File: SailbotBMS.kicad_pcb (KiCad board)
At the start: 2 copper layers, 5 parts, among them J1 Conn_01x05_Female, J2 Conn_01x02, J3 Conn_01x02, U1 BQ77915

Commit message: still incorrect footprint for transistor
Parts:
- removed C1: C, Capacitor_SMD:C_0603_1608Metric
- removed J1: Conn_01x05_Female, Connector_JST:JST_XH_B05B-XH-AM_1x05_P2.50mm_Vertical
- removed J2: Conn_01x02, TerminalBlock_Phoenix:TerminalBlock_Phoenix_MKDS-1,5-2-5.08_1x02_P5.08mm_Horizontal
- removed J3: Conn_01x02, Connector_PinHeader_2.54mm:PinHeader_1x02_P2.54mm_Vertical
- removed U1: BQ77915, Package_SO:TSSOP-24_4.4x7.8mm_P0.65mm

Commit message: change footprint for transistors - maybe still not right
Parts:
- added C1: 1uF, Capacitor_SMD:C_0603_1608Metric, F.Cu at (75.2, 57.7)
- added C2: 1uF, Capacitor_SMD:C_0603_1608Metric, F.Cu at (81.2, 57.7)
- added C3: 1uF, Capacitor_SMD:C_0603_1608Metric, F.Cu at (87.2, 56.2)
- added C4: 1uF, Capacitor_SMD:C_0603_1608Metric, F.Cu at (84.2, 56.2)
- added C5: 1uF, Capacitor_SMD:C_0603_1608Metric, F.Cu at (81.2, 56.2)
- added C_VDD1: 1uF, Capacitor_SMD:C_0603_1608Metric, F.Cu at (61.0, 59.8)
- added C_VDO1: 1uF, Capacitor_SMD:C_0603_1608Metric, F.Cu at (76.1, 59.2)
- added J1: Conn_01x05_Female, Connector_JST:JST_XH_B05B-XH-AM_1x05_P2.50mm_Vertical, F.Cu at (121.9, 43.2)
- added J2: Conn_01x02, TerminalBlock_Phoenix:TerminalBlock_Phoenix_MKDS-1,5-2-5.08_1x02_P5.08mm_Horizontal, F.Cu at (62.6, 46.8)
- added J3: Conn_01x02, Connector_PinHeader_2.54mm:PinHeader_1x02_P2.54mm_Vertical, F.Cu at (99.6, 36.1)
- added Q_NMOS_CHG1: Q2, Package_TO_SOT_SMD:TO-252-3_TabPin2, F.Cu at (87.5, 51.9)
- added Q_NMOS_CHG2: Q2, Package_TO_SOT_SMD:TO-252-3_TabPin2, F.Cu at (87.5, 44.9)
- added Q_NMOS_CHG3: Q2, Package_TO_SOT_SMD:TO-252-3_TabPin2, F.Cu at (76.3, 51.9)
- added Q_NMOS_CHG4: Q2, Package_TO_SOT_SMD:TO-252-3_TabPin2, F.Cu at (92.2, 37.8)
- added Q_NMOS_DGS1: Q, Package_TO_SOT_SMD:TO-252-3_TabPin2, F.Cu at (76.3, 44.9)
- added Q_NMOS_DGS2: Q, Package_TO_SOT_SMD:TO-252-3_TabPin2, F.Cu at (65.1, 55.5)
- added Q_NMOS_DGS3: Q, Package_TO_SOT_SMD:TO-252-3_TabPin2, F.Cu at (81.1, 37.8)
- added Q_NMOS_DGS4: Q, Package_TO_SOT_SMD:TO-252-3_TabPin2, F.Cu at (106.7, 50.8)
- added R1: 33, Resistor_SMD:R_0603_1608Metric, F.Cu at (64.0, 59.8)
- added R2: 33, Resistor_SMD:R_0603_1608Metric, F.Cu at (67.1, 59.8)
- added R3: 33, Resistor_SMD:R_0603_1608Metric, F.Cu at (70.1, 59.8)
- added R4: 33, Resistor_SMD:R_0603_1608Metric, F.Cu at (72.2, 56.2)
- added R5: 33, Resistor_SMD:R_0603_1608Metric, F.Cu at (72.2, 57.7)
- added R_CB1: 10k, Resistor_SMD:R_0603_1608Metric, F.Cu at (75.2, 56.2)
- added R_CHG1: 1k, Resistor_SMD:R_0603_1608Metric, F.Cu at (78.2, 56.2)
- added R_DSG1: 4.5k, Resistor_SMD:R_0603_1608Metric, F.Cu at (73.1, 59.2)
- added R_GS1: 1M, Resistor_SMD:R_0603_1608Metric, F.Cu at (84.2, 57.7)
- added R_GS2: 1M, Resistor_SMD:R_0603_1608Metric, F.Cu at (102.9, 35.0)
- added R_LD1: 470k, Resistor_SMD:R_0603_1608Metric, F.Cu at (78.2, 57.7)
- added R_OCD1: R, Resistor_SMD:R_0603_1608Metric, F.Cu at (102.9, 38.1)
- added R_SNS1: 100m, Resistor_SMD:R_0603_1608Metric, F.Cu at (102.9, 36.6)
- added R_TS_PU1: 10k, Resistor_SMD:R_0603_1608Metric, F.Cu at (82.1, 59.2)
- added R_VDD1: 1k, Resistor_SMD:R_0603_1608Metric, F.Cu at (79.1, 59.2)
- added TH1: 103AT, 10k, Resistor_SMD:R_0402_1005Metric, F.Cu at (72.5, 60.5)
- added U1: BQ77915, Package_SO:TSSOP-24_4.4x7.8mm_P0.65mm, F.Cu at (127.0, 63.5)

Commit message: initial layout
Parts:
- moved J1 71.5 mm to (53.3, 63.5), turned to 90 degrees
- moved Q_NMOS_DGS4 59.9 mm to (55.9, 82.5)
- moved Q_NMOS_DGS3 46.4 mm to (68.6, 82.5)
- moved U1 43.8 mm to (83.8, 55.9)
- moved Q_NMOS_DGS1 41.6 mm to (94.0, 82.5)
- moved R_GS2 38.7 mm to (77.5, 64.1)
- moved Q_NMOS_CHG1 37.6 mm to (55.9, 72.4)
- moved R_SNS1 36.1 mm to (72.4, 55.9)
- moved Q_NMOS_CHG4 34.6 mm to (94.0, 72.4)
- moved Q_NMOS_CHG2 33.4 mm to (68.6, 72.4)
- moved Q_NMOS_DGS2 31.5 mm to (81.3, 82.5)
- moved J2 30.7 mm to (92.7, 52.7)
- moved R_OCD1 29.9 mm to (88.3, 64.1)
- moved J3 25.5 mm to (97.8, 61.6)
- moved TH1 21.5 mm to (94.0, 59.7)
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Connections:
- R1 pad 1: Net-(C5-Pad1) -> Net-(C1-Pad2)
- R1 pad 2: PACK+ -> Net-(J1-Pad1)
- R2 pad 1: Net-(C4-Pad1) -> Net-(C2-Pad1)
- R2 pad 2: Net-(J1-Pad4) -> Net-(J1-Pad2)
- R4 pad 1: Net-(C2-Pad1) -> Net-(C4-Pad1)
- R4 pad 2: Net-(J1-Pad2) -> Net-(J1-Pad4)
- R5 pad 1: Net-(C1-Pad2) -> Net-(C5-Pad1)
- R5 pad 2: Net-(J1-Pad1) -> PACK+

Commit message: afternoon check-in
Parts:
- R_OCD1: value R -> 750k
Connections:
- R_OCD1 pad 2: GNDREF -> PACK+
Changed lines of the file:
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@@
       (effects (font (size 1 1) (thickness 0.15)))
     )
-    (fp_text value R (at 0 1.43) (layer F.Fab)
+    (fp_text value 750k (at 0 1.43) (layer F.Fab)
       (effects (font (size 1 1) (thickness 0.15)))
     )
@@
       (net 31 "Net-(R_OCD1-Pad1)"))
     (pad 2 smd roundrect (at 0.7875 0) (size 0.875 0.95) (layers F.Cu F.Paste F.Mask) (roundrect_rratio 0.25)
-      (net 1 GNDREF))
+      (net 13 PACK+))
     (model ${KISYS3DMOD}/Resistor_SMD.3dshapes/R_0603_1608Metric.wrl
       (at (xyz 0 0 0))

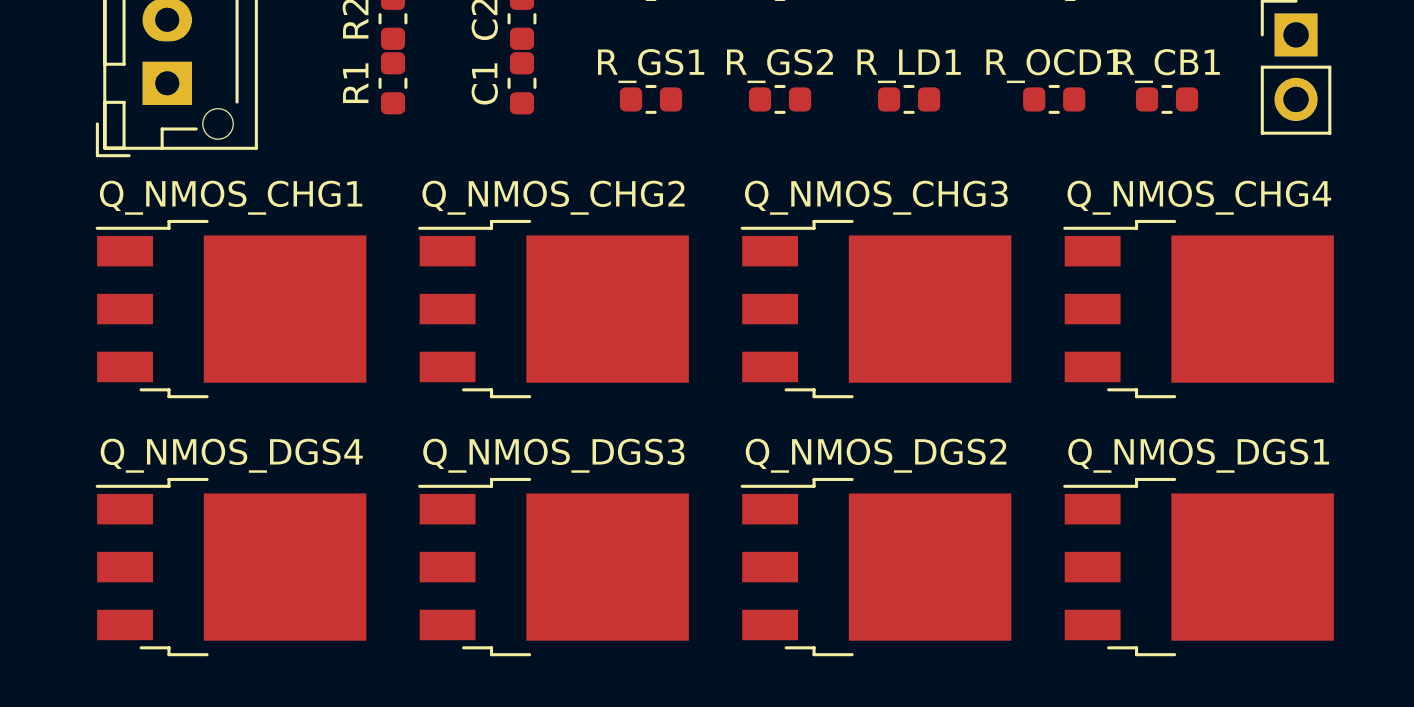
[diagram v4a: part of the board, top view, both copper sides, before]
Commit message: renaming so it makes more sense to me
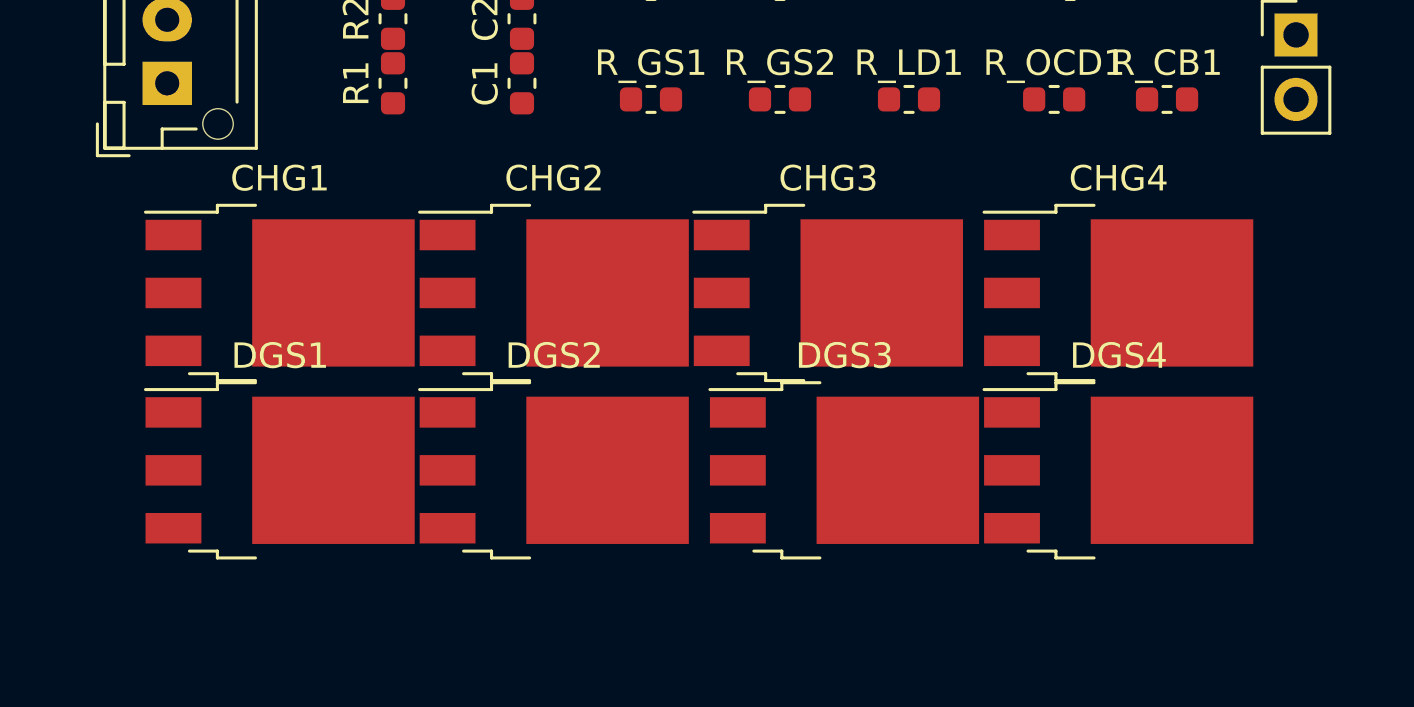
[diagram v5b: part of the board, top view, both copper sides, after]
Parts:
- removed Q_NMOS_CHG1, Q_NMOS_CHG2, Q_NMOS_CHG3, Q_NMOS_CHG4: Q2, Package_TO_SOT_SMD:TO-252-3_TabPin2
- removed Q_NMOS_DGS1, Q_NMOS_DGS2, Q_NMOS_DGS3, Q_NMOS_DGS4: Q, Package_TO_SOT_SMD:TO-252-3_TabPin2
- added CHG1: Q2, Package_TO_SOT_SMD:TO-252-3_TabPin2, F.Cu at (57.8, 71.8)
- added CHG2: Q2, Package_TO_SOT_SMD:TO-252-3_TabPin2, F.Cu at (68.6, 71.8)
- added CHG3: Q2, Package_TO_SOT_SMD:TO-252-3_TabPin2, F.Cu at (79.4, 71.8)
- added CHG4: Q2, Package_TO_SOT_SMD:TO-252-3_TabPin2, F.Cu at (90.8, 71.8)
- added DGS1: Q, Package_TO_SOT_SMD:TO-252-3_TabPin2, F.Cu at (57.8, 78.7)
- added DGS2: Q, Package_TO_SOT_SMD:TO-252-3_TabPin2, F.Cu at (68.6, 78.7)
- added DGS3: Q, Package_TO_SOT_SMD:TO-252-3_TabPin2, F.Cu at (80.0, 78.7)
- added DGS4: Q, Package_TO_SOT_SMD:TO-252-3_TabPin2, F.Cu at (90.8, 78.7)
- R_OCD1: value 750k -> 196k
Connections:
- R_OCD1 pad 2: PACK+ -> GNDREF

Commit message: end of day commit
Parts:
- removed J3: Conn_01x02, Connector_PinHeader_2.54mm:PinHeader_1x02_P2.54mm_Vertical
- added R_GSC1: 1M, Resistor_SMD:R_0603_1608Metric, F.Cu at (112.4, 47.7)
- added R_GSC2: 1M, Resistor_SMD:R_0603_1608Metric, F.Cu at (112.4, 49.2)
- added R_GSC3: 1M, Resistor_SMD:R_0603_1608Metric, F.Cu at (115.4, 47.7)
- added R_GSC4: 1M, Resistor_SMD:R_0603_1608Metric, F.Cu at (112.4, 50.7)
- added R_GSD1: 1M, Resistor_SMD:R_0603_1608Metric, F.Cu at (115.4, 49.2)
- added R_GSD2: 1M, Resistor_SMD:R_0603_1608Metric, F.Cu at (118.4, 47.7)
- added R_GSD3: 1M, Resistor_SMD:R_0603_1608Metric, F.Cu at (115.4, 50.7)
- added R_GSD4: 1M, Resistor_SMD:R_0603_1608Metric, F.Cu at (118.4, 49.2)
- CHG1, CHG2, CHG3, CHG4: value Q2 -> 4V
- DGS1, DGS2, DGS3, DGS4: value Q -> 4V
- R_CHG1: value 1k -> 0
- R_DSG1: value 4.5k -> 0
- R_SNS1: value 100m -> 4m
- moved DGS4 4.96 mm to (94.0, 82.5)
- moved DGS1 4.26 mm to (55.9, 82.5)
- moved DGS3 4.02 mm to (81.3, 82.5)
- moved DGS2 3.81 mm to (68.6, 82.5)
- moved CHG4 3.24 mm to (94.0, 72.4)
- moved CHG3 2.01 mm to (81.3, 72.4)
- moved CHG1 2.01 mm to (55.9, 72.4)
- moved CHG2 0.64 mm to (68.6, 72.4)
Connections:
- C1 pad 1: GNDREF -> PACK-
- C2 pad 2: GNDREF -> PACK-
- CHG2 pad 1: Net-(CHG2-Pad1) -> Net-(CHG1-Pad1)
- CHG2 pad 3: Net-(CHG1-Pad1) -> PACK-
- CHG3 pad 1: Net-(CHG3-Pad1) -> Net-(CHG1-Pad1)
- CHG3 pad 3: Net-(CHG2-Pad1) -> PACK-
- CHG4 pad 1: Net-(CHG4-Pad1) -> Net-(CHG1-Pad1)
- CHG4 pad 3: Net-(CHG3-Pad1) -> PACK-
- C_VDD1 pad 2: GNDREF -> PACK-
- C_VDO1 pad 2: GNDREF -> PACK-
- DGS1 pad 1: Net-(DGS1-Pad1) -> Net-(CHG1-Pad1)
- DGS2 pad 1: Net-(DGS2-Pad1) -> Net-(CHG1-Pad1)
- DGS2 pad 3: Net-(DGS1-Pad1) -> Net-(DGS1-Pad3)
- DGS3 pad 1: Net-(DGS3-Pad1) -> Net-(CHG1-Pad1)
- DGS3 pad 3: Net-(DGS2-Pad1) -> Net-(DGS1-Pad3)
- DGS4 pad 1: Net-(CHG4-Pad1) -> Net-(CHG1-Pad1)
- DGS4 pad 3: Net-(DGS3-Pad1) -> Net-(DGS1-Pad3)
- R_CB1 pad 2: GNDREF -> PACK-
- R_OCD1 pad 2: GNDREF -> PACK-
- TH1 pad 1: GNDREF -> PACK-
- U1 pad 22: PRES -> PACK+
- U1 pad 23: GNDREF -> PACK-
- U1 pad 24: GNDREF -> PACK-
